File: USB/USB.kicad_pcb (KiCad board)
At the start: 4 copper layers, 70 x 60 mm, 24 parts, among them J1 USBC-4-0-CX90MW9-24P1, U2 ESDA25L, U3 USB SWITCH 2CHANNEL TS3USB221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, U6 usb-polarity-TUSB321RWBR

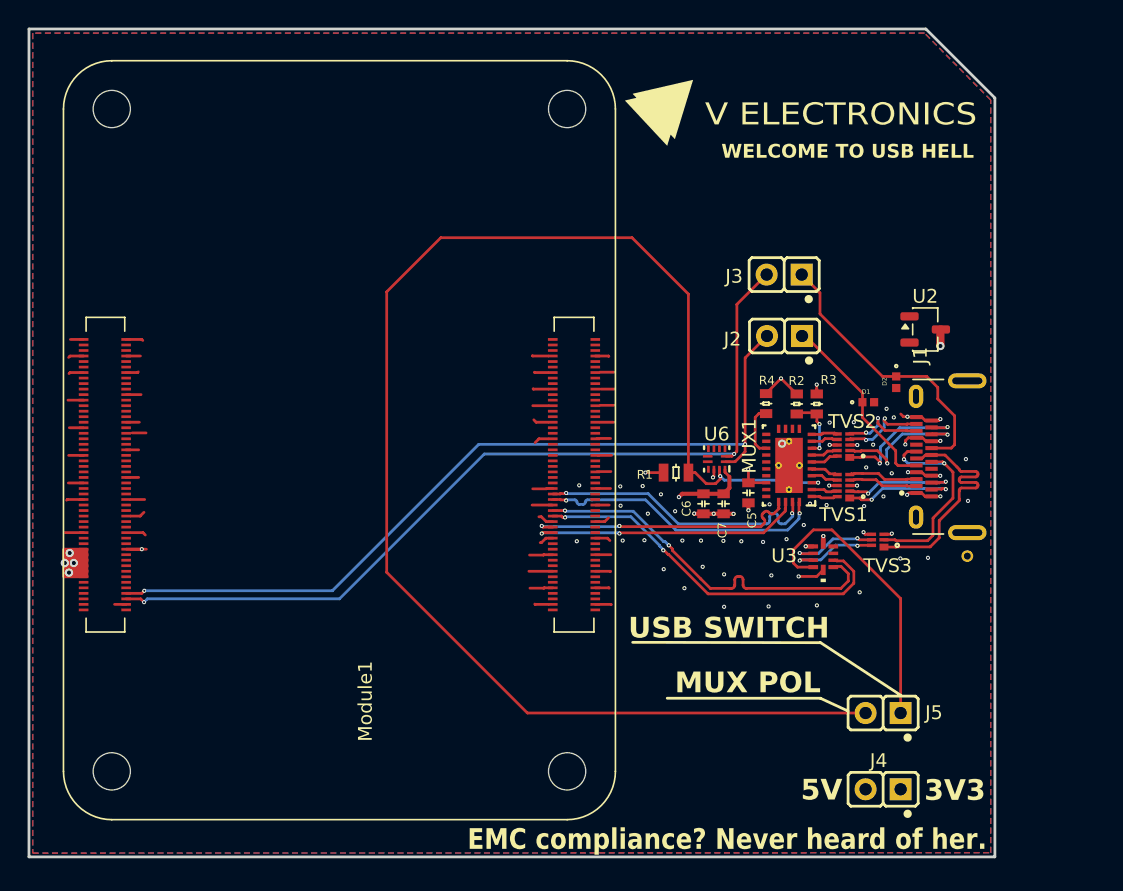
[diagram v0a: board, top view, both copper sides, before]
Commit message: add GND test point
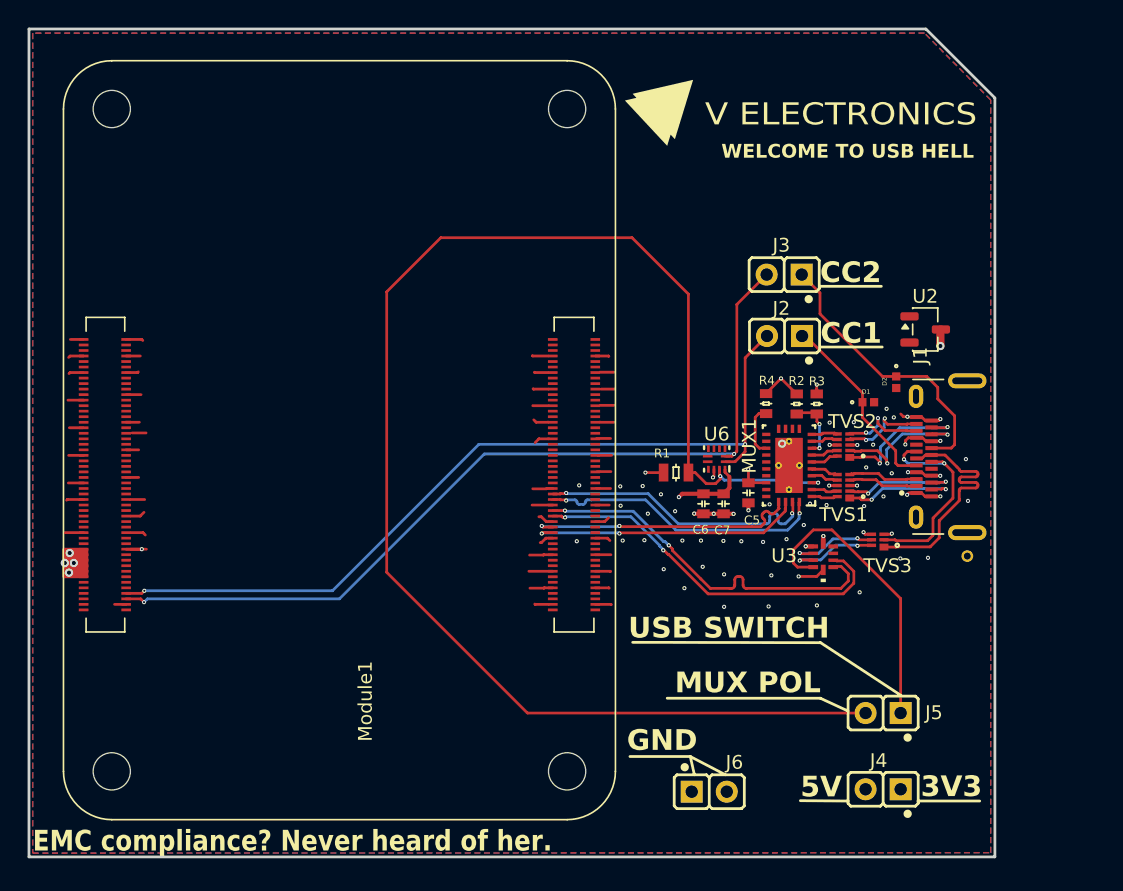
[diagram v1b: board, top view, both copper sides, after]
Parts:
- added J6: ~, COMATEL THD:COMATEL_385.0358.1.02.400, F.Cu at (108.0, 115.3)
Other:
- board text added: "CC1"
- board text added: "CC2"
- board text added: "GND"

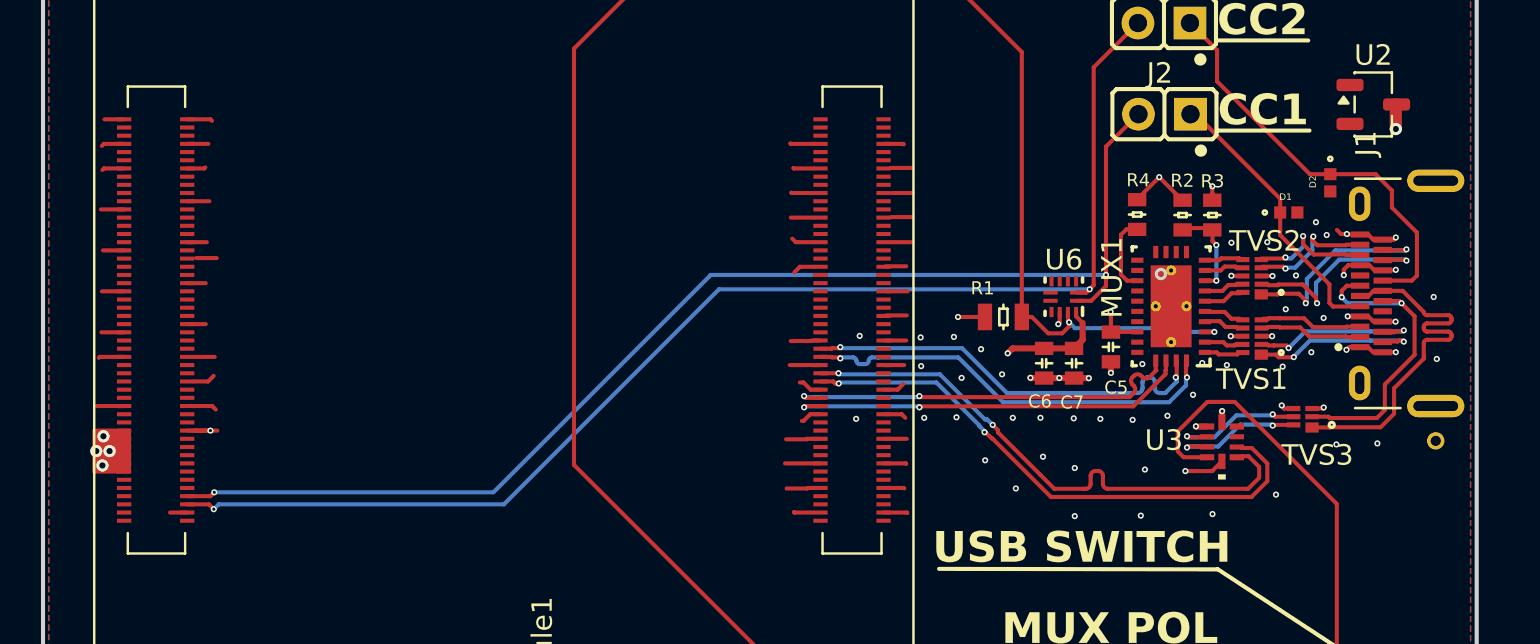
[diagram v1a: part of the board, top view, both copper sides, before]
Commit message: increase via annular ring size for PCBWAY manufacturing
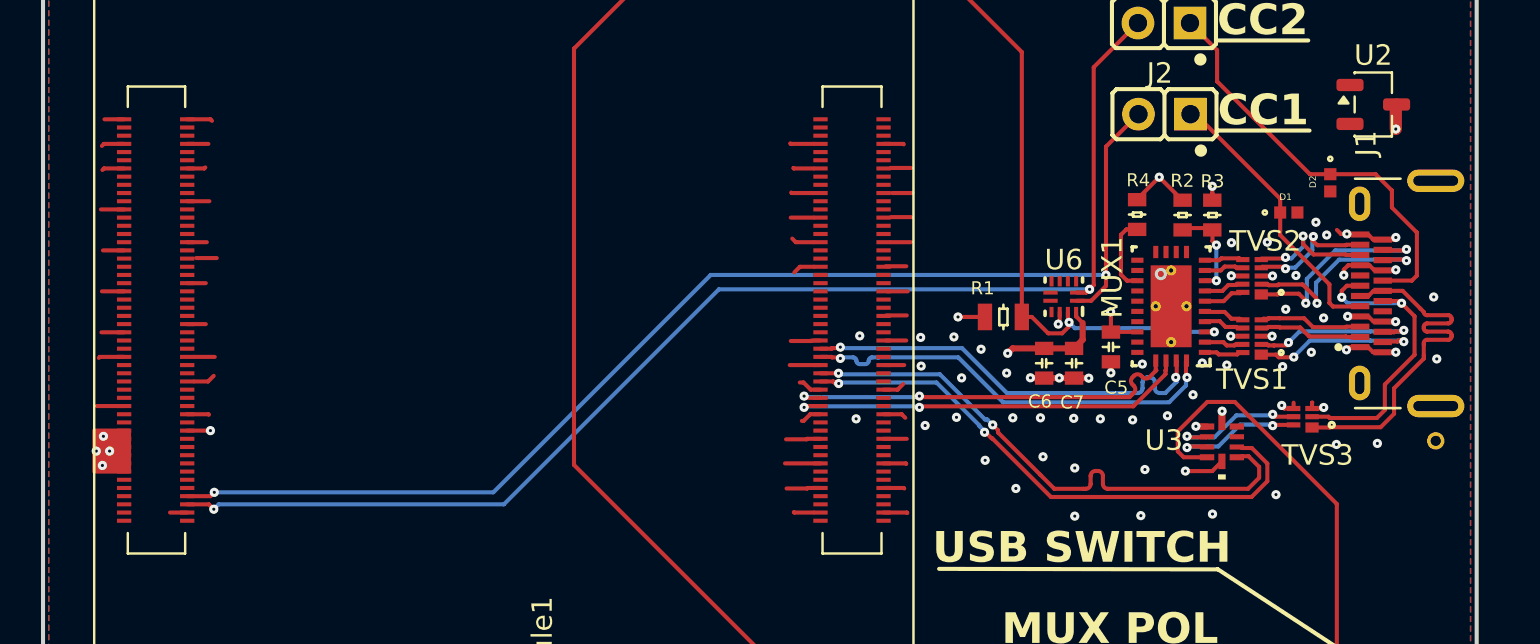
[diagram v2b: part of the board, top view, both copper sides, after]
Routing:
- net GND: track 69.7 -> 71.4 mm
- net 3V3B: track 11.0 -> 9.87 mm
- net unconnected-(Module1A-SD_DAT6-Pad72): track 1.13 -> 0.00 mm

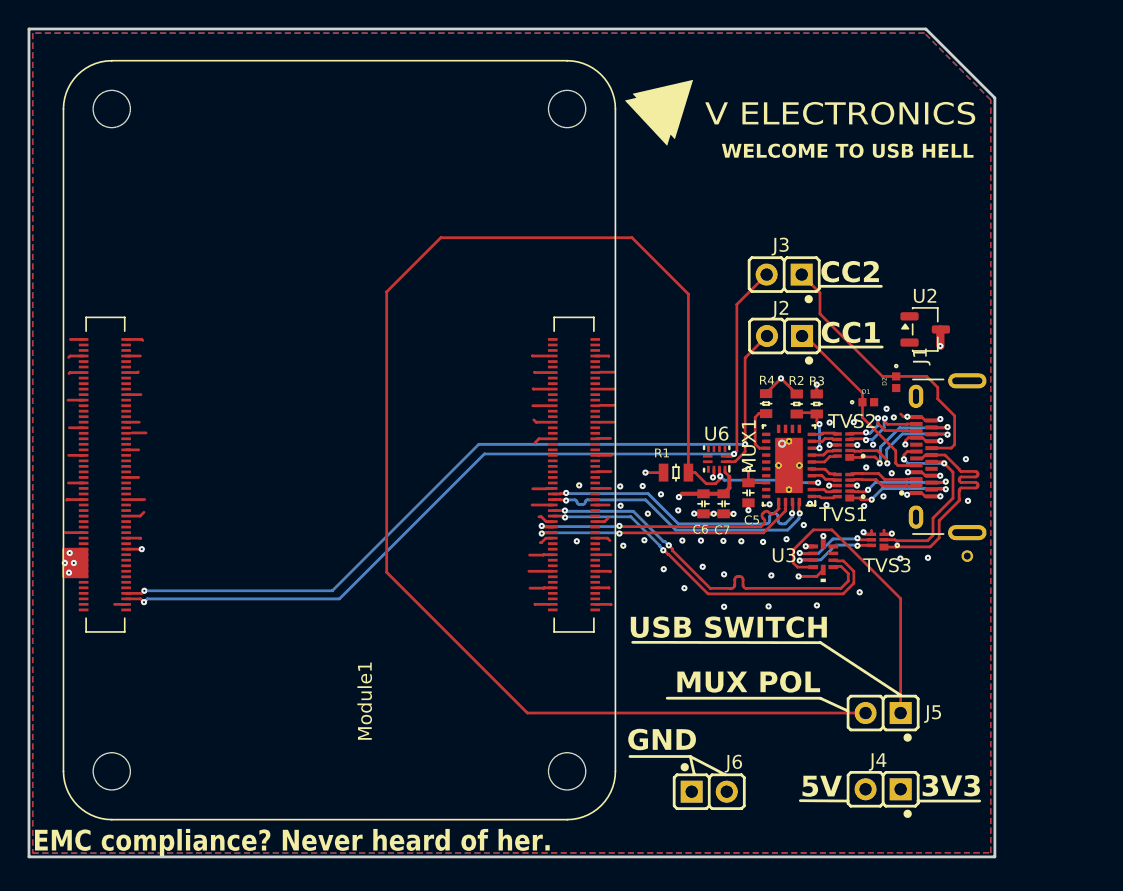
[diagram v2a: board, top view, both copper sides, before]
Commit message: fix some DRC issues
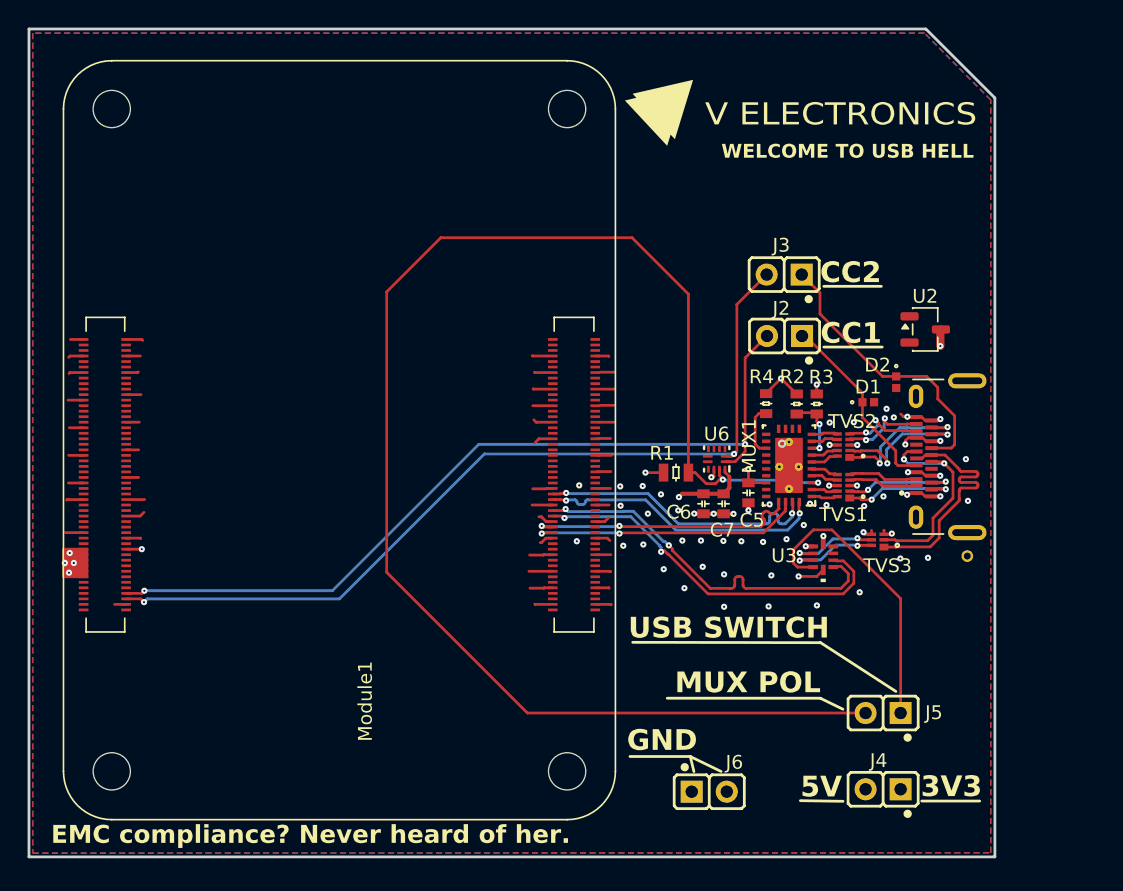
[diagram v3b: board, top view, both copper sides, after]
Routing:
- net unconnected-(Module1A-ID_SD-Pad36): track 1.01 -> 0.00 mm
- net GND: track 71.4 -> 71.5 mm, vias 60 -> 57

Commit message: add patreon supporters names
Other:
- board text added: "Supporters: Cifer Setsuna Terran Earthling Tom Thiery Emanuel Stradex Hjalte Hansen"
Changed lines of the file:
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@@
 		(capping no)
 		(filling no)
-		(zone_defaults)
 		(pcbplotparams
 			(layerselection 0x00000000_00000000_55555555_5755f5ff)
@@
 		)
 	)
+	(gr_text "Supporters:\nCifer\nSetsuna\nTerran Earthling\nTom \nThiery Emanuel\nStradex\nHjalte Hansen\n"
+		(at 124.28 73.83 0)
+		(layer "B.SilkS")
+		(effects
+			(font
+				(size 1 1)
+				(thickness 0.125)
+			)
+			(justify left bottom mirror)
+		)
+	)

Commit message: engi 2026-08-13 voicechat review
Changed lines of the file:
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@@
 			(layer "F.Paste")
-		)
-		(fp_circle
-			(center 0.5 1.576393)
-			(end 0.7 1.676393)
-			(stroke
-				(width 0.15)
-				(type solid)
-			)
-			(fill no)
-			(layer "Edge.Cuts")
 		)
 		(fp_line
@@
 		)
 		(pad "29" thru_hole circle
-			(at -0.7 -0.1 180)
-			(size 0.6 0.6)
-			(drill 0.2)
+			(at -0.7 -0.5 180)
+			(size 0.6 0.6)
+			(drill 0.2)
+			(property pad_prop_heatsink)
+			(layers "*.Cu" "*.Mask")
+			(remove_unused_layers no)
+			(net "GND")
+			(pinfunction "PAD_GND_29")
+			(pintype "power_in")
+		)
+		(pad "29" thru_hole circle
+			(at -0.7 0.5 180)
+			(size 0.6 0.6)
+			(drill 0.2)
+			(property pad_prop_heatsink)
 			(layers "*.Cu" "*.Mask")
 			(remove_unused_layers no)
@@
 			(size 0.6 0.6)
 			(drill 0.2)
+			(property pad_prop_heatsink)
+			(layers "*.Cu" "*.Mask")
+			(remove_unused_layers no)
+			(net "GND")
+			(pinfunction "PAD_GND_29")
+			(pintype "power_in")
+		)
+		(pad "29" thru_hole circle
+			(at 0 0 180)
+			(size 0.6 0.6)
+			(drill 0.2)
+			(property pad_prop_heatsink)
 			(layers "*.Cu" "*.Mask")
 			(remove_unused_layers no)
@@
 			(size 0.6 0.6)
 			(drill 0.2)
-			(layers "*.Cu" "*.Mask")
-			(remove_unused_layers no)
-			(net "GND")
-			(pinfunction "PAD_GND_29")
-			(pintype "power_in")
-		)
-		(pad "29" thru_hole circle
-			(at 0.7 -0.1 180)
-			(size 0.6 0.6)
-			(drill 0.2)
-			(layers "*.Cu" "*.Mask")
-			(remove_unused_layers no)
+			(property pad_prop_heatsink)
+			(layers "*.Cu" "*.Mask")
+			(remove_unused_layers no)
+			(net "GND")
+			(pinfunction "PAD_GND_29")
+			(pintype "power_in")
+		)
+		(pad "29" thru_hole circle
+			(at 0.7 -0.5 180)
+			(size 0.6 0.6)
+			(drill 0.2)
+			(property pad_prop_heatsink)
+			(layers "*.Cu" "*.Mask")
+			(remove_unused_layers no)
+			(net "GND")
+			(pinfunction "PAD_GND_29")
+			(pintype "power_in")
+		)
+		(pad "29" thru_hole circle
+			(at 0.7 0.5 180)
+			(size 0.6 0.6)
+			(drill 0.2)
+			(property pad_prop_heatsink)
+			(layers "*.Cu" "*.Mask")
+			(remove_unused_layers no)

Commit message: add packaging info, remove bad fields, format BOM for PCBWAY
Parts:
- TVS3: value ~ -> 2 Line Common Mode Choke with ESD 100mA DCR 6Ohm
